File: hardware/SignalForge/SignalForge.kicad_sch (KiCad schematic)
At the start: 36 parts, among them J1 Micro_SD_Card_Det2, P1 USB_C_Plug_USB2.0, SW1 SW_Push, U2 W25Q32JVSS, U3 USBLC6-2SC6, U4 SPX3819M5-L-3-3, U5 ESP32-S3, Y1 40MHz

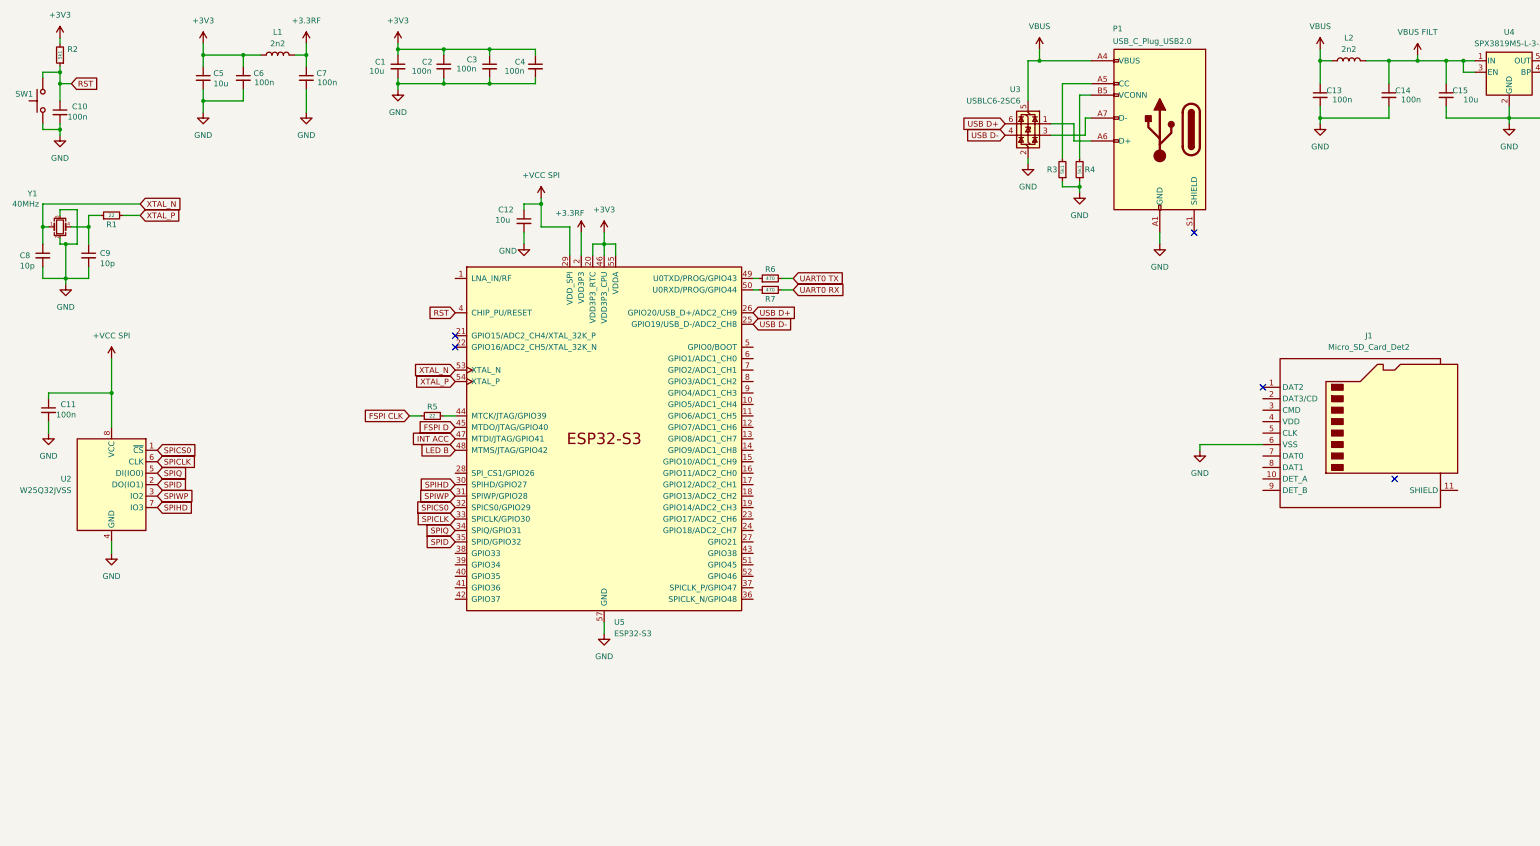
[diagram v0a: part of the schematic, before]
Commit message: sw: sdcard, camera
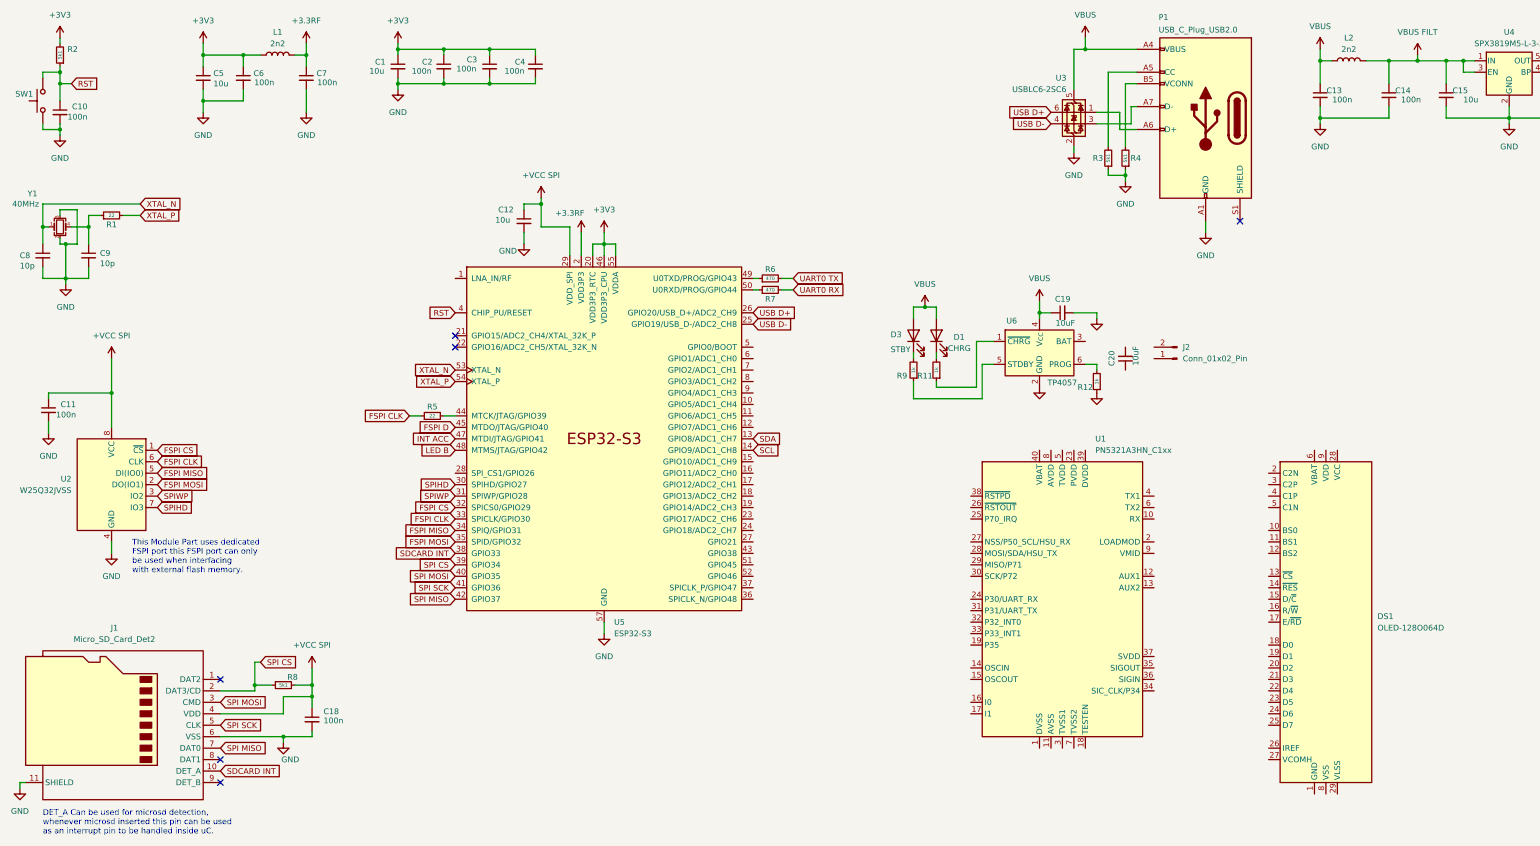
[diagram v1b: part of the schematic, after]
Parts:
- added C18: 100n, symbol Device:C_Small
- added C19, C20: 10uF, symbol Device:C_Small
- added D1: CHRG, symbol Device:LED
- added D3: STBY, symbol Device:LED
- added DS1: OLED-128O064D, Display:OLED-128O064D, symbol Display_Graphic:OLED-128O064D
- added J2: Conn_01x02_Pin, symbol Connector:Conn_01x02_Pin
- added R11, R12, R9: 1k, symbol Device:R_Small
- added R8: 5k1, symbol Device:R_Small
- added U1: PN5321A3HN_C1xx, Package_DFN_QFN:HVQFN-40-1EP_6x6mm_P0.5mm_EP4.1x4.1mm, symbol RF_NFC:PN5321A3HN_C1xx
- added U6: TP4057, Package_TO_SOT_SMD:TSOT-23-5, symbol Battery_Management:TP4057
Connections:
- net SPICLK is gone; now on net FSPI CLK: U2.6 (CLK), U5.33 (SPICLK/GPIO30)
- net +VCC SPI: now also J1.4 (VDD), C18.1, R8.2
- net GND: now also J1.11 (SHIELD), C18.2, C19.2, R12.1, U6.2 (GND)
- net VBUS: now also C19.1, D1.2 (A), D3.2 (A), U6.4 (V_{CC})
- net SDCARD INT: now reaches J1.10 (DET_A)
- net SDCARD INT: now also U5.38 (GPIO33)
- net SPI CS: now reaches J1.2 (DAT3/CD)
- net SPI CS: now also U5.39 (GPIO34), R8.1
- net SPI MOSI: now reaches J1.3 (CMD)
- net SPI MOSI: now also U5.40 (GPIO35)
- net SPI SCK: now reaches J1.5 (CLK)
- net SPI SCK: now also U5.41 (GPIO36)
- net SPI MISO: now reaches J1.7 (DAT0)
- net SPI MISO: now also U5.42 (GPIO37)
- net SDA: now reaches U5.13 (GPIO8/ADC1_CH7)
- net SCL: now reaches U5.14 (GPIO9/ADC1_CH8)
- net SPICS0 renamed FSPI CS
- net SPID renamed FSPI MOSI
- net SPIQ renamed FSPI MISO
- new net: R11.1, U6.1 (~{CHRG})
- new net: R9.1, U6.5 (STDBY)
- new net: R12.2, U6.6 (PROG)
- new net: DS1.1 (GND), DS1.30 (GND)
- new net: D3.1 (K), R9.2
- new net: D1.1 (K), R11.2
- new net: U1.11 (AVSS), U1.41 (AVSS)
- no-connect marks 5 -> 6
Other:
- note added: "DET_A Can be used for microsd detection, whenever microsd inserted this pin can be used as an interrupt pin to be handled inside uC."
- note added: "This Module Part uses dedicated FSPI port this FSPI port can only be used when interfacing with external flash memory."
- moved on the sheet: J1, P1, R3, R4, U3

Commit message: feat: ir, nfc, battery charger
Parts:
- removed DS1: OLED-128O064D, Display:OLED-128O064D, symbol Display_Graphic:OLED-128O064D
- removed J2: Conn_01x02_Pin, symbol Connector:Conn_01x02_Pin
- added BT1: Battery_Cell, symbol Device:Battery_Cell
- added C21, C23, C24, C25, C26: 100n, symbol Device:C_Small
- added C22, C40: 10uF, symbol Device:C_Small
- added C27, C30, C32: 22p, symbol Device:C_Small
- added C28, C31: 220p, symbol Device:C_Small
- added C29, C33: 100p, symbol Device:C_Small
- added C34, C35, C36, C37: NC, symbol Device:C_Small
- added C38: 1nF, symbol Device:C_Small
- added C39: 10u, symbol Device:C_Small
- added C41: 2.2u, symbol Device:C_Small
- added D4: IR204A, LED_THT:LED_D3.0mm_IRBlack, symbol LED:IR204A
- added L3, L4: 560n, symbol Device:L
- added Q1: AO3400A, Package_TO_SOT_SMD:SOT-23, symbol Transistor_FET:AO3400A
- added R13, R14: 4k7, symbol Device:R_Small
- added R15, R16: 1.5, symbol Device:R_Small
- added R17, R18: NC, symbol Device:R_Small
- added R19, R20, R21: 1k, symbol Device:R_Small
- added R22: 33, symbol Device:R_Small
- added U7: DM-OLED096-636, DM-OLED096-636:MODULE_DM-OLED096-636, symbol DM-OLED096-636:DM-OLED096-636
- added U8: TSDP343xx, OptoDevice:Vishay_MOLD-3Pin, symbol Interface_Optical:TSDP343xx
- added Y2: 27.12MHz, symbol Device:Crystal
- C20: value 10uF -> 22p
- D2: value LED -> PWRLED
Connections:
- net +3V3: now also U1.17 (I1), U1.23 (PVDD), C24.1, C41.1, R13.2, R14.2, R22.2, U7.2 (VCC_IN), U8.3 (Vs)
- net GND: now also C20.2, U1.1 (DVSS), U1.11 (AVSS), U1.16 (I0), U1.18 (TESTEN), U1.3 (TVSS1), U1.41 (AVSS), U1.7 (TVSS2), U1.9 (VMID), BT1.2 (-), C21.2, C22.2, C23.2, C24.2, C25.2, C26.2, C27.2, C28.2, C29.2, C31.2, C33.2, C34.2, C35.1, C39.2, C40.2, C41.2, D4.1 (K), R17.2, R18.1, R19.2, U7.1 (GND), U8.2 (GND)
- net SCL: now also U5.9 (GPIO4/ADC1_CH3), R14.1, U7.3 (SCL); no longer U5.14 (GPIO9/ADC1_CH8)
- net SDA: now also U5.10 (GPIO5/ADC1_CH4), R13.1, U7.4 (SDA); no longer U5.13 (GPIO8/ADC1_CH7)
- net at C20.1: now also U1.14 (OSCIN), Y2.2
- net +BATT: now reaches U6.3 (BAT)
- net +BATT: now also U1.40 (VBAT), BT1.1 (+)
- net at U1.10 (RX): now also C38.2, R19.1
- net AUX1: now reaches U1.12 (AUX1)
- net AUX2: now reaches U1.13 (AUX2)
- net at U1.15 (OSCOUT): now also C27.1, Y2.1
- net NFC_IRQ: now reaches U1.25 (P70_IRQ)
- net NFC_NSS/SCL/RX: now reaches U1.27 (NSS/P50_SCL/HSU_RX)
- net NFC_MOSI/SDA/TX: now reaches U1.28 (MOSI/SDA/HSU_TX)
- net NFC_MISO: now reaches U1.29 (MISO/P71)
- net NFC_SCK: now reaches U1.30 (SCK/P72)
- net at U1.37 (SVDD): now also C40.1
- net RSTPD_N: now reaches U1.38 (~{RSTPD})
- net VCC NFC: now reaches U1.39 (DVDD)
- net VCC NFC: now also U1.5 (TVDD), U1.8 (AVDD), C21.1, C22.1, C23.1, C25.1, C26.1, C39.1
- net at U1.4 (TX1): now also L3.1
- net at U1.6 (TX2): now also L4.1
- new net: C28.1, C30.1, C37.1, L3.2, R20.1
- new net: C38.1, R20.2
- new net: D4.2 (A), Q1.2 (S)
- new net: C31.1, C32.1, C36.1, L4.2
- new net: C32.2, C33.1, C35.2, C36.2, R16.2
- new net: C29.1, C30.2, C34.1, C37.2, R15.2
- new net: Q1.3 (D), R22.1
- new net: Q1.1 (G), R21.1
- new net IR_RX: U8.1 (OUT)
- new net IR_TX: R21.2
- new net TX1: R15.1, R17.1
- new net TX2: R16.1, R18.2
- no-connect marks 6 -> 16
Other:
- note added: "BATTERY CHARGER"
- note added: "CRYSTAL for ESP32"
- note added: "DECOUPLING FOR ESP32"
- note added: "DECOUPLING FOR ESP32-RF"
- note added: "EXTERNAL FLASH MEMORY"
- note added: "IR TRANSCEIVER"
- note added: "MICROCONTROLLER ESP32"
- note added: "NFC MODULE (PN532)"
- note added: "OLED_SSD1306_128x64"
- note added: "REGULATOR 3.3V"
- note added: "RST_PIN FOR ESP32"
- note added: "SEL0 -> 0 SEL1 -> 1 (SPI HOST)"
- note added: "SLOT MICROSD"
- note added: "USB-C/UART/PROGRAMMER"
- moved on the sheet: C1, C10, C11, C12, C13, C14, C15, C16, C17, C18, C19, C2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
